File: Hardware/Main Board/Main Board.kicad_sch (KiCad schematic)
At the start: 7 parts, among them SW1 SW_SPST, U1 ESP32-S3-WROOM-2

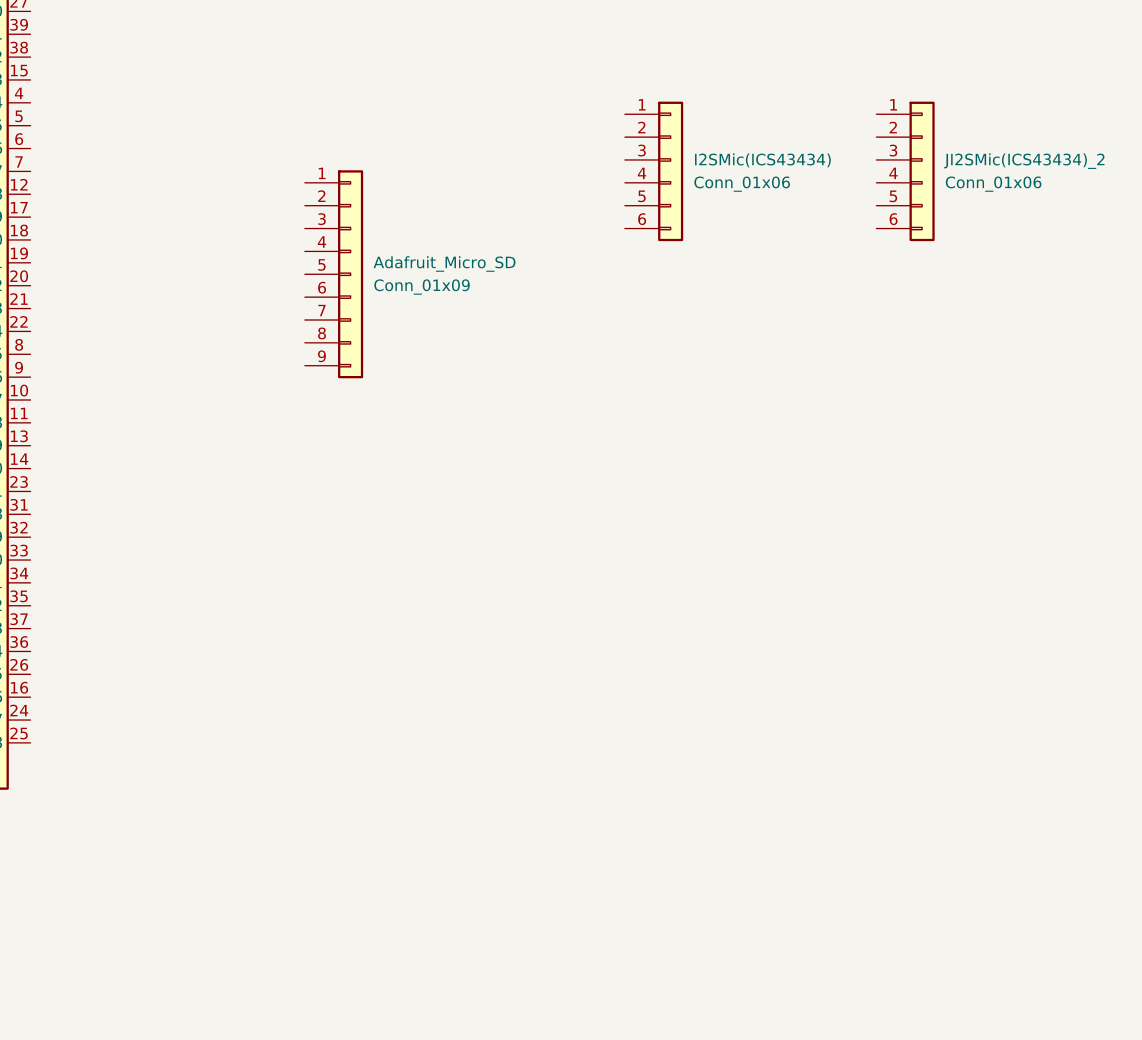
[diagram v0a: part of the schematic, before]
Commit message: SD card schematic
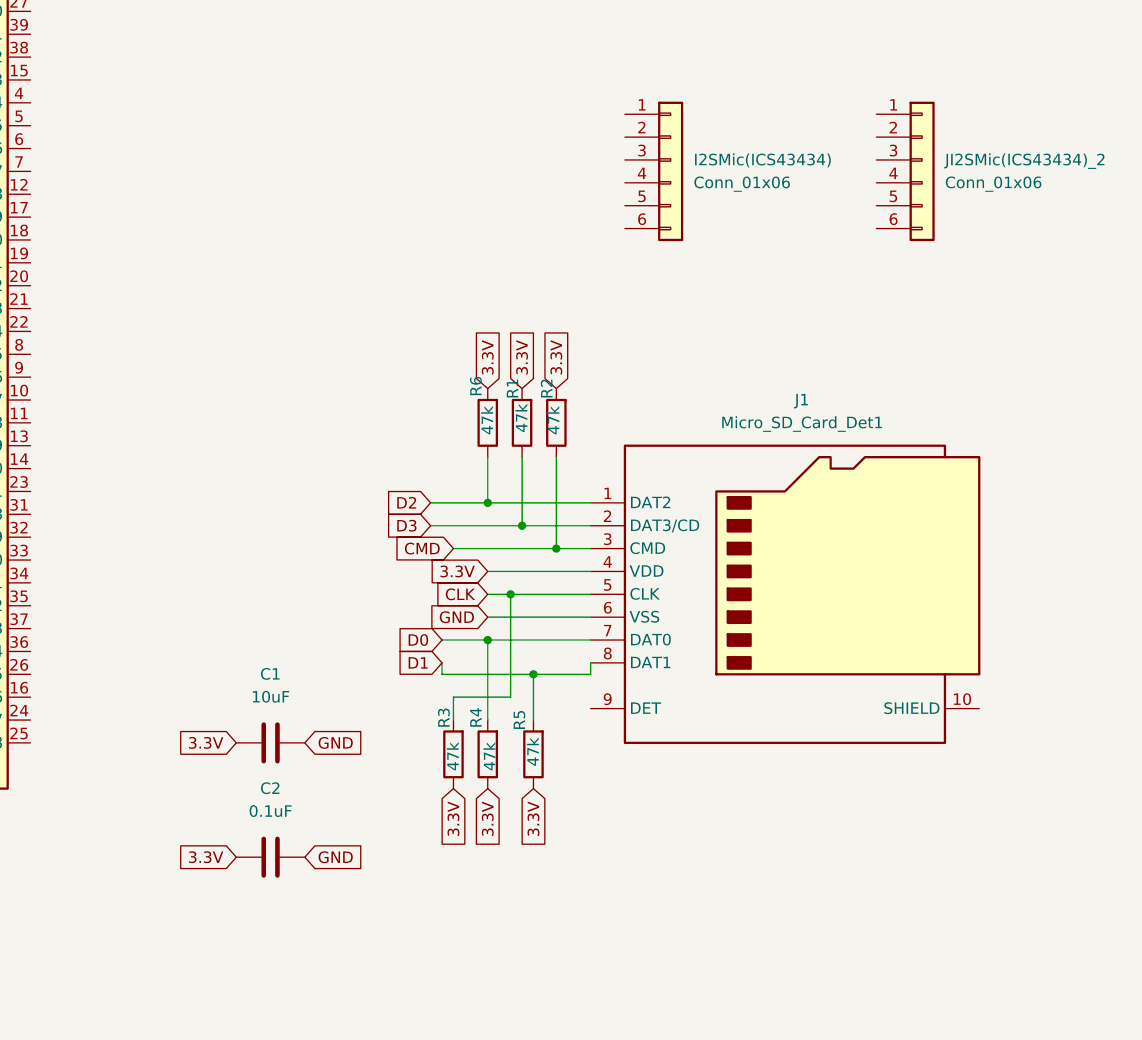
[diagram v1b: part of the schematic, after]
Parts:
- removed Adafruit_Micro_SD: Conn_01x09, symbol Connector_Generic:Conn_01x09
- added C1: 10uF, symbol Device:C
- added C2: 0.1uF, symbol Device:C
- added J1: Micro_SD_Card_Det1, symbol Connector:Micro_SD_Card_Det1
- added R1, R2, R3, R4, R5, R6: 47k, symbol Device:R
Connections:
- new net 3.3V: C1.2, C2.1, J1.4 (VDD), R1.2, R2.2, R3.1, R4.1, R5.1, R6.2
- new net CLK: J1.5 (CLK), R3.2
- new net CMD: J1.3 (CMD), R2.1
- new net D0: J1.7 (DAT0), R4.2
- new net D1: J1.8 (DAT1), R5.2
- new net D2: J1.1 (DAT2), R6.1
- new net D3: J1.2 (DAT3/CD), R1.1
- new net GND: C1.1, C2.2, J1.6 (VSS)

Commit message: reviewed main board work done by Kevin
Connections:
- net 3.3V: no longer C1.2, C2.1, R1.2, R2.2, R3.1, R4.1, R5.1, R6.2
- net GND: now also C1.2, C2.1, U1.1 (GND), U1.40 (GND), U1.41 (GND); no longer C1.1, C2.2
- net +3.3V: now reaches U1.2 (3V3)
- net +3.3V: now also C1.1, C2.2, R1.2, R2.2, R3.1, R4.1, R5.1, R6.2
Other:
- moved on the sheet: C1, C2

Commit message: schematics for oled and mics
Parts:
- removed I2SMic(ICS43434), JI2SMic(ICS43434)_2: Conn_01x06, symbol Connector_Generic:Conn_01x06
- removed OLED: Conn_01x04, symbol Connector_Generic:Conn_01x04
- added C3, C5: 1uF, symbol Device:C
- added C4, C6: 220pF, symbol Device:C
- added MK1, MK2: ICS-43434, Sensor_Audio:InvenSense_ICS-43434-6_3.5x2.65mm, symbol Sensor_Audio:ICS-43434
- added R10, R7: 68, symbol Device:R
- added R8, R9: 10k, symbol Device:R
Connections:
- net +3.3V: now also C3.1, C4.1, C5.1, C6.1, MK1.5 (VDD), MK2.5 (VDD)
- net GND: now also C3.2, C4.2, C5.2, C6.2, MK1.3 (GND), MK2.3 (GND), R8.2, R9.2
- new net: MK2.6 (SD), R10.1
- new net: MK1.6 (SD), R7.1
- new net BCLK: MK1.4 (SCK)
- new net BCLK2: MK2.4 (SCK)
- new net DATA: R7.2
- new net DATA2: R10.2
- new net SELECT: MK1.2 (LR), R8.1
- new net SELECT2: MK2.2 (LR), R9.1
- new net WS: MK1.1 (WS)
- new net WS2: MK2.1 (WS)
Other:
- added sheet OLED (Adafruit OLED 128x32 Mono I2C STEMMA QT rev B/Adafruit OLED 128x32 Mono I2C STEMMA QT rev B.kicad_sch)
- moved on the sheet: BZ1, C1, C2, J1, R1, R2, R3, R4, R5, R6, SW1, U1
